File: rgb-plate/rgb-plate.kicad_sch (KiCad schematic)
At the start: 0 parts

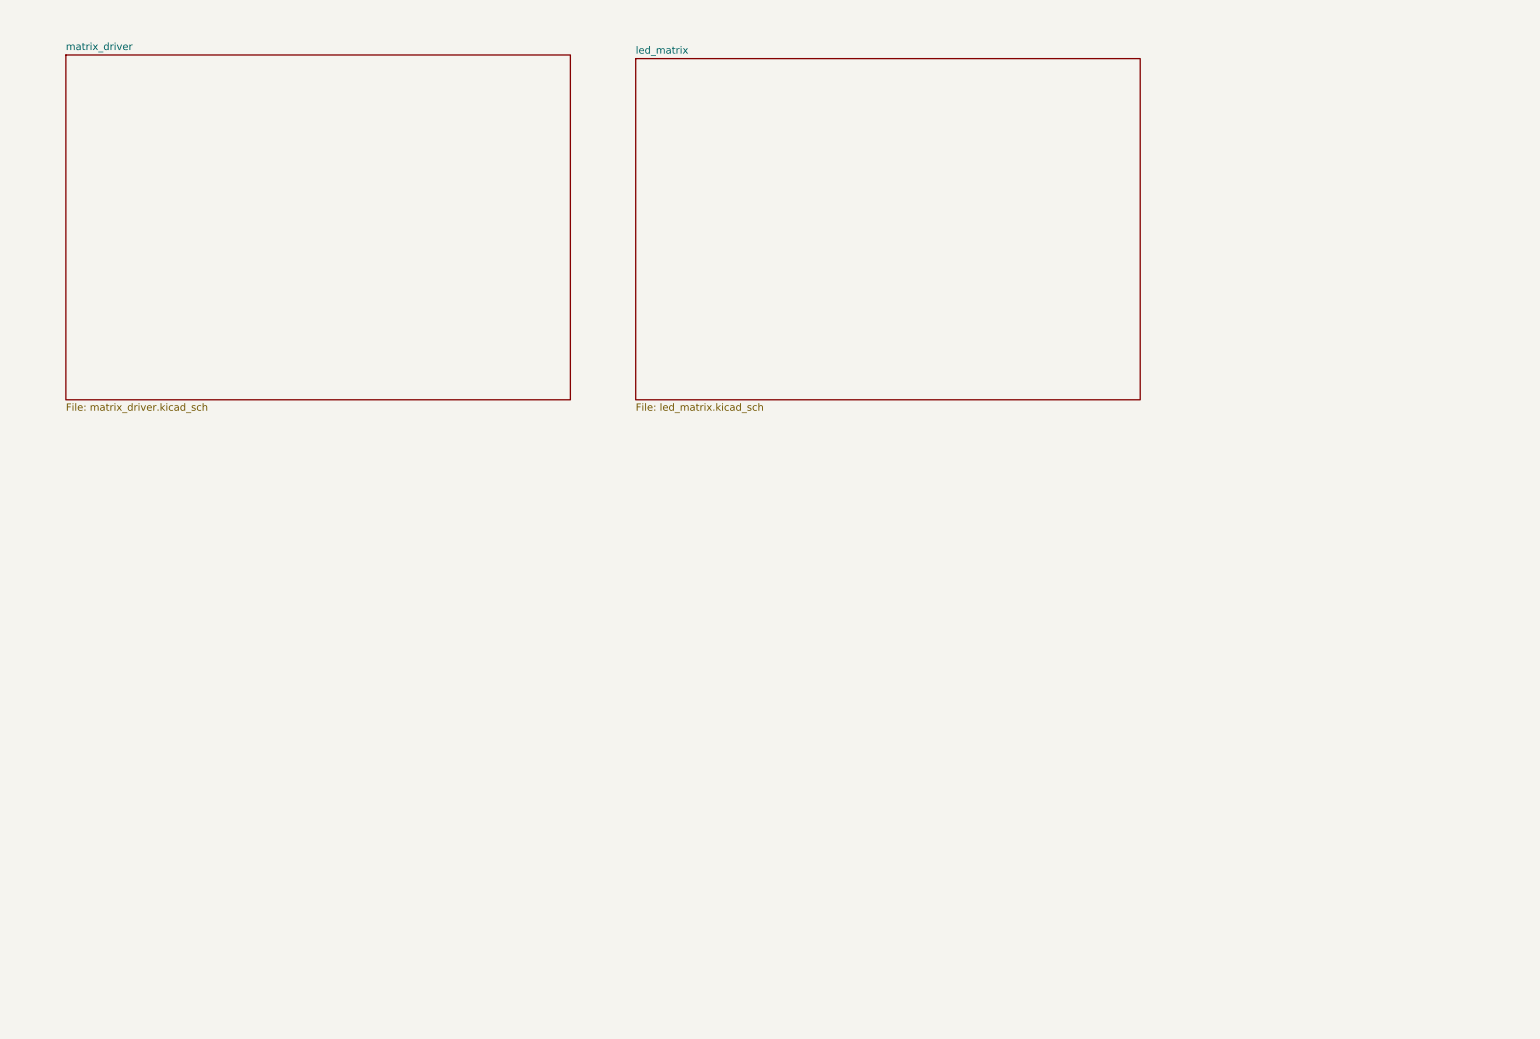
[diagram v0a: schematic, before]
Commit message: added additional sheets and leds with matrix driver and first regulator
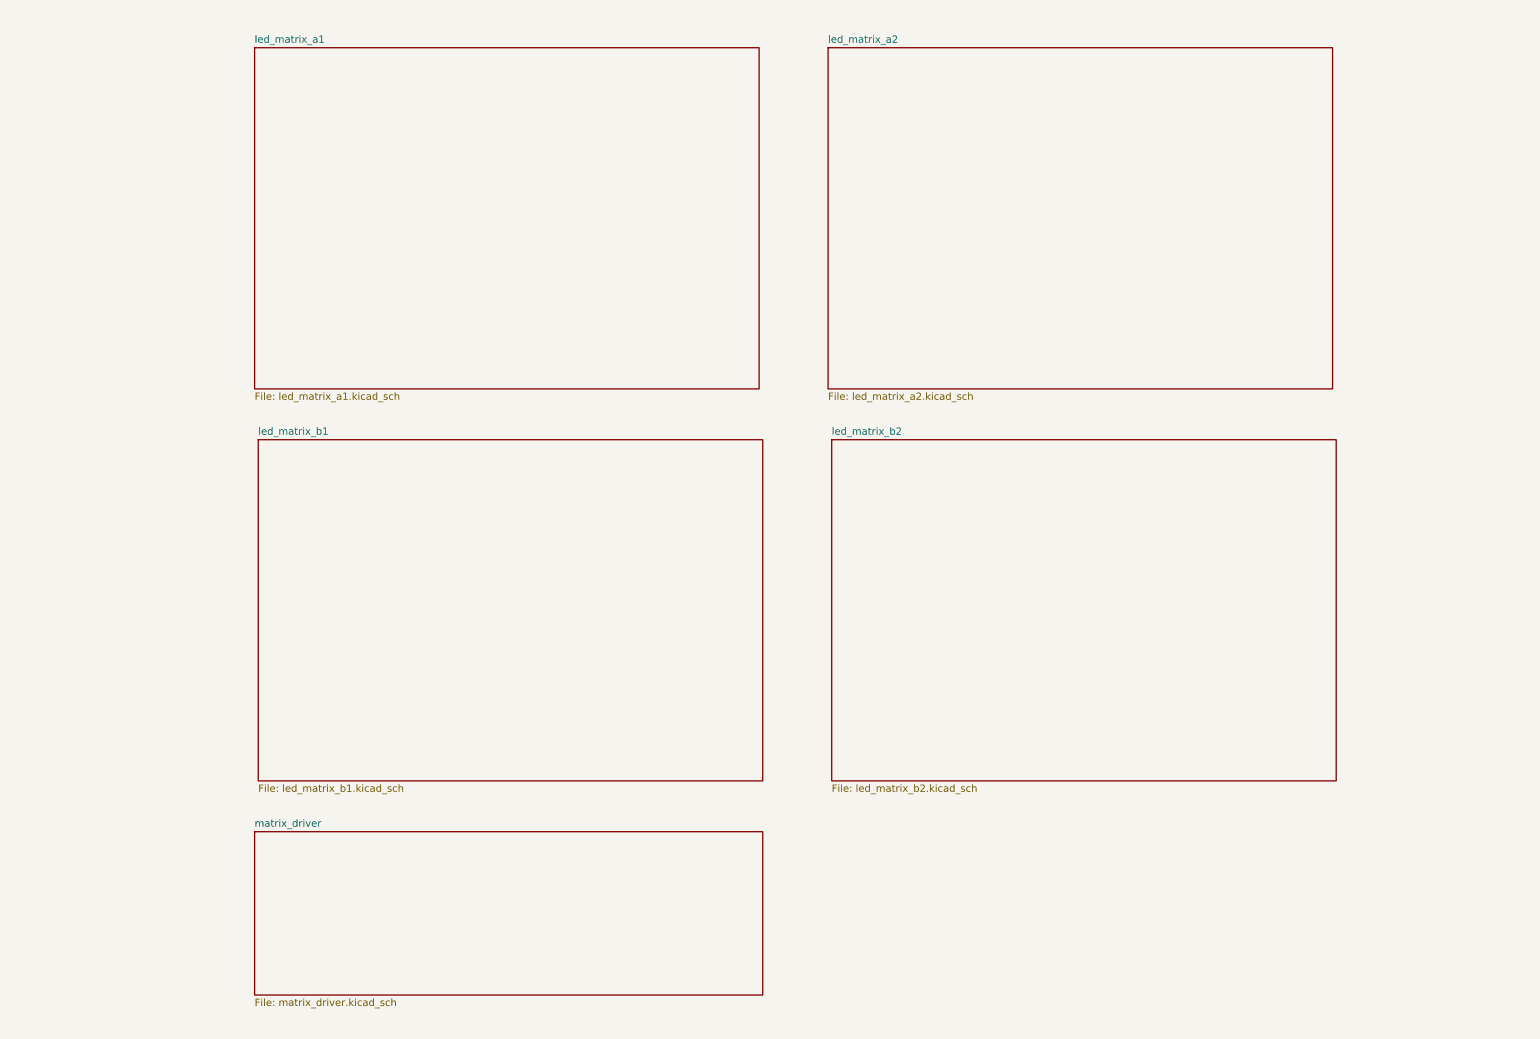
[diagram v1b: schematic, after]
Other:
- sheet led_matrix renamed led_matrix_a1
- added sheet led_matrix_a2 (led_matrix_a2.kicad_sch)
- added sheet led_matrix_b1 (led_matrix_b1.kicad_sch)
- added sheet led_matrix_b2 (led_matrix_b2.kicad_sch)
- sheet led_matrix_a1: file led_matrix.kicad_sch -> led_matrix_a1.kicad_sch
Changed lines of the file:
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@@
 	(paper "A4")
 	(sheet
-		(at 26.035 24.13)
-		(size 88.265 60.325)
+		(at 59.055 160.02)
+		(size 88.9 28.575)
 		(exclude_from_sim no)
 		(in_bom yes)
@@
 		)
 		(property "Sheetname" "matrix_driver"
-			(at 26.035 23.4184 0)
+			(at 59.055 159.3084 0)
 			(effects
 				(font
@@
 		)
 		(property "Sheetfile" "matrix_driver.kicad_sch"
-			(at 26.035 85.0396 0)
+			(at 59.055 189.1796 0)
 			(effects
 				(font
@@
 	)
 	(sheet
-		(at 125.73 24.765)
-		(size 88.265 59.69)
-		(exclude_from_sim no)
-		(in_bom yes)
-		(on_board yes)
-		(dnp no)
-		(fields_autoplaced yes)
-		(stroke
-			(width 0.1524)
-			(type solid)
-		)
-		(fill
-			(color 0 0 0 0.0000)
-		)
-		(property "Sheetname" "led_matrix"
-			(at 125.73 24.0534 0)
-			(effects
-				(font
-					(size 1.27 1.27)
-				)
-				(justify left bottom)
-			)
-		)
-		(property "Sheetfile" "led_matrix.kicad_sch"
-			(at 125.73 85.0396 0)
+		(at 59.055 22.86)
+		(size 88.265 59.69)
+		(exclude_from_sim no)
+		(in_bom yes)
+		(on_board yes)
+		(dnp no)
+		(fields_autoplaced yes)
+		(stroke
+			(width 0.1524)
+			(type solid)
+		)
+		(fill
+			(color 0 0 0 0.0000)
+		)
+		(property "Sheetname" "led_matrix_a1"
+			(at 59.055 22.1484 0)
+			(effects
+				(font
+					(size 1.27 1.27)
+				)
+				(justify left bottom)
+			)
+		)
+		(property "Sheetfile" "led_matrix_a1.kicad_sch"
+			(at 59.055 83.1346 0)
 			(effects
 				(font
@@
 				)
 			)
+		)
+	)
+	(sheet
+		(at 160.02 91.44)
+		(size 88.265 59.69)
+		(exclude_from_sim no)
+		(in_bom yes)
+		(on_board yes)
+		(dnp no)
+		(fields_autoplaced yes)
+		(stroke
+			(width 0.1524)
+			(type solid)
+		)
+		(fill
+			(color 0 0 0 0.0000)
+		)
+		(property "Sheetname" "led_matrix_b2"
+			(at 160.02 90.7284 0)
+			(effects
+				(font
+					(size 1.27 1.27)
+				)
+				(justify left bottom)
+			)
+		)
+		(property "Sheetfile" "led_matrix_b2.kicad_sch"
+			(at 160.02 151.7146 0)
+			(effects
+				(font
+					(size 1.27 1.27)
+				)
+				(justify left top)
+			)
+		)
+		(instances
+			(project "rgb-plate"
+				(path "/9c7e9324-2b76-44c1-9f0e-b92eb5faec31"
+					(page "6")
+				)
+			)
+		)
+	)
+	(sheet
+		(at 159.385 22.86)
+		(size 88.265 59.69)
+		(exclude_from_sim no)
+		(in_bom yes)
+		(on_board yes)
+		(dnp no)
+		(fields_autoplaced yes)
+		(stroke
+			(width 0.1524)
+			(type solid)
+		)
+		(fill
+			(color 0 0 0 0.0000)
+		)
+		(property "Sheetname" "led_matrix_a2"
+			(at 159.385 22.1484 0)
+			(effects
+				(font
+					(size 1.27 1.27)
+				)
+				(justify left bottom)
+			)
+		)
+		(property "Sheetfile" "led_matrix_a2.kicad_sch"
+			(at 159.385 83.1346 0)
+			(effects
+				(font
+					(size 1.27 1.27)
+				)
+				(justify left top)
+			)
+		)
+		(instances
+			(project "rgb-plate"
+				(path "/9c7e9324-2b76-44c1-9f0e-b92eb5faec31"
+					(page "4")
+				)
+			)
+		)
+	)
+	(sheet
+		(at 59.69 91.44)
+		(size 88.265 59.69)
+		(exclude_from_sim no)
+		(in_bom yes)
+		(on_board yes)
+		(dnp no)
+		(fields_autoplaced yes)
+		(stroke
+			(width 0.1524)
+			(type solid)
+		)
+		(fill
+			(color 0 0 0 0.0000)
+		)
+		(property "Sheetname" "led_matrix_b1"
+			(at 59.69 90.7284 0)
+			(effects
+				(font
+					(size 1.27 1.27)
+				)
+				(justify left bottom)
+			)
+		)
+		(property "Sheetfile" "led_matrix_b1.kicad_sch"
+			(at 59.69 151.7146 0)
+			(effects
+				(font
+					(size 1.27 1.27)
+				)
+				(justify left top)
+			)
+		)
+		(instances
+			(project "rgb-plate"
+				(path "/9c7e9324-2b76-44c1-9f0e-b92eb5faec31"
+					(page "5")
+				)
+			)

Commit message: initial layout on single board, may need to split up
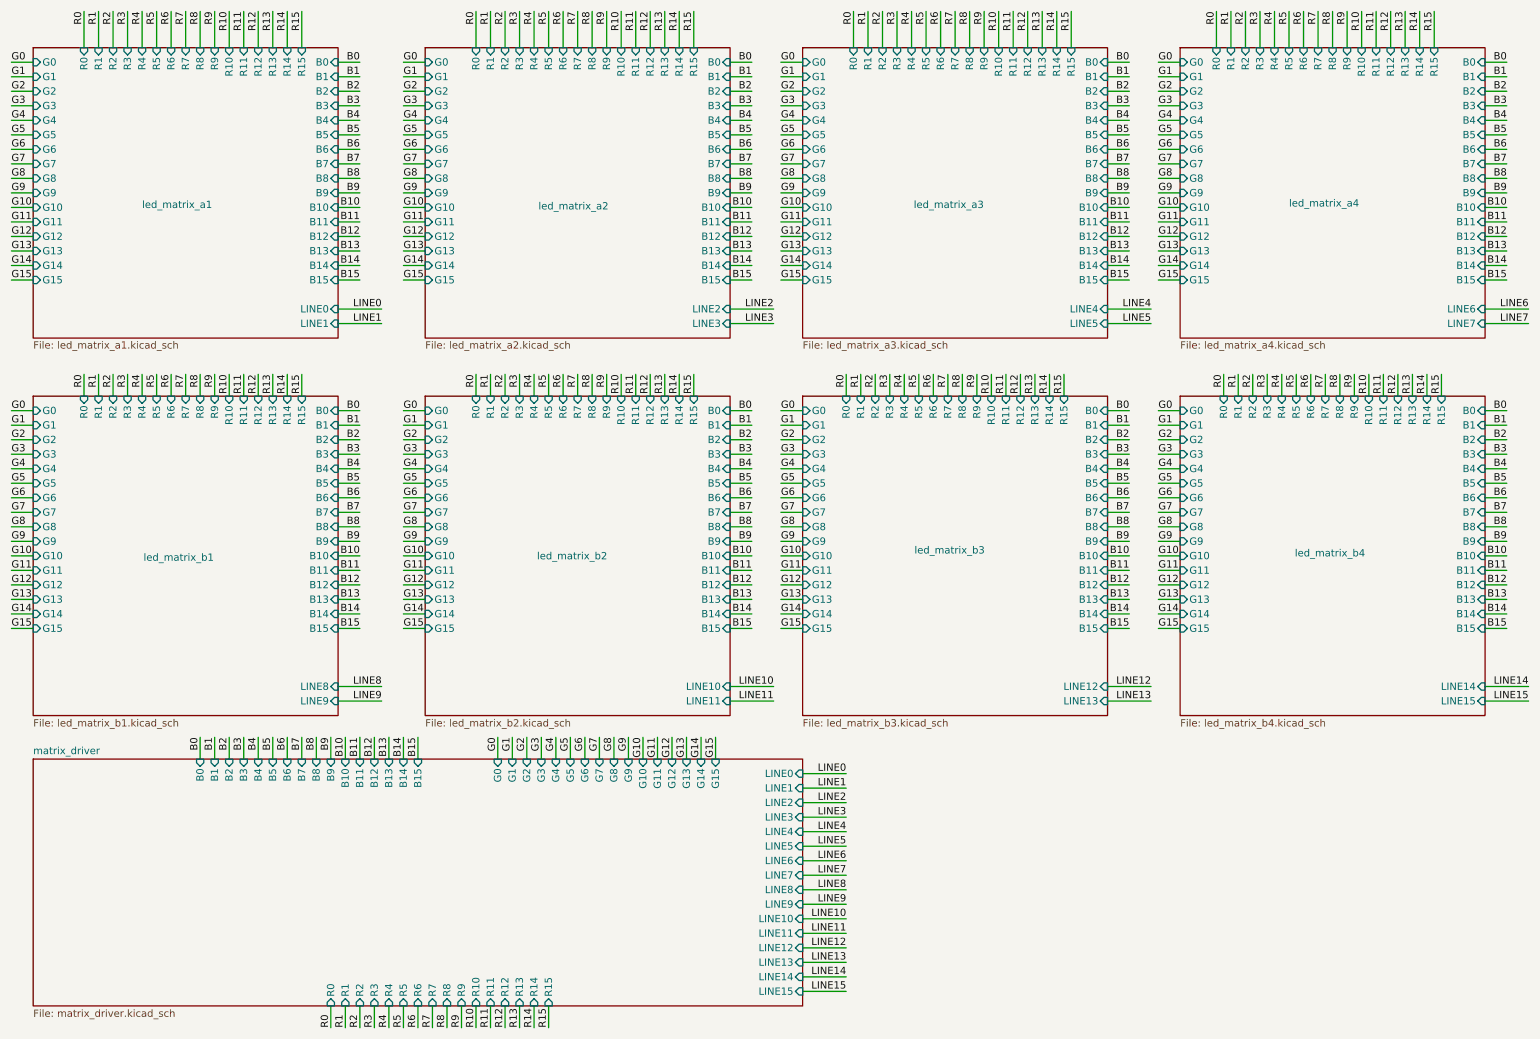
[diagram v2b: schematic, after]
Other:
- added sheet led_matrix_a3 (led_matrix_a3.kicad_sch)
- added sheet led_matrix_a4 (led_matrix_a4.kicad_sch)
- added sheet led_matrix_b3 (led_matrix_b3.kicad_sch)
- added sheet led_matrix_b4 (led_matrix_b4.kicad_sch)
- sheet led_matrix_a1 ports: added B0, B1, B10, B11, B12, B13, B14, B15, B2, B3, B4, B5, B6, B7, B8, B9, G0, G1, G10, G11, G12, G13, G14, G15, G2, G3, G4, G5, G6, G7, G8, G9, LINE0, LINE1, R0, R1, R10, R11, R12, R13, R14, R15, R2, R3, R4, R5, R6, R7, R8, R9; removed none
- sheet led_matrix_a2 ports: added B0, B1, B10, B11, B12, B13, B14, B15, B2, B3, B4, B5, B6, B7, B8, B9, G0, G1, G10, G11, G12, G13, G14, G15, G2, G3, G4, G5, G6, G7, G8, G9, LINE2, LINE3, R0, R1, R10, R11, R12, R13, R14, R15, R2, R3, R4, R5, R6, R7, R8, R9; removed none
- sheet led_matrix_b1 ports: added B0, B1, B10, B11, B12, B13, B14, B15, B2, B3, B4, B5, B6, B7, B8, B9, G0, G1, G10, G11, G12, G13, G14, G15, G2, G3, G4, G5, G6, G7, G8, G9, LINE8, LINE9, R0, R1, R10, R11, R12, R13, R14, R15, R2, R3, R4, R5, R6, R7, R8, R9; removed none
- sheet led_matrix_b2 ports: added B0, B1, B10, B11, B12, B13, B14, B15, B2, B3, B4, B5, B6, B7, B8, B9, G0, G1, G10, G11, G12, G13, G14, G15, G2, G3, G4, G5, G6, G7, G8, G9, LINE10, LINE11, R0, R1, R10, R11, R12, R13, R14, R15, R2, R3, R4, R5, R6, R7, R8, R9; removed none
- sheet matrix_driver ports: added B0, B1, B10, B11, B12, B13, B14, B15, B2, B3, B4, B5, B6, B7, B8, B9, G0, G1, G10, G11, G12, G13, G14, G15, G2, G3, G4, G5, G6, G7, G8, G9, LINE0, LINE1, LINE10, LINE11, LINE12, LINE13, LINE14, LINE15, LINE2, LINE3, LINE4, LINE5, LINE6, LINE7, LINE8, LINE9, R0, R1, R10, R11, R12, R13, R14, R15, R2, R3, R4, R5, R6, R7, R8, R9; removed none

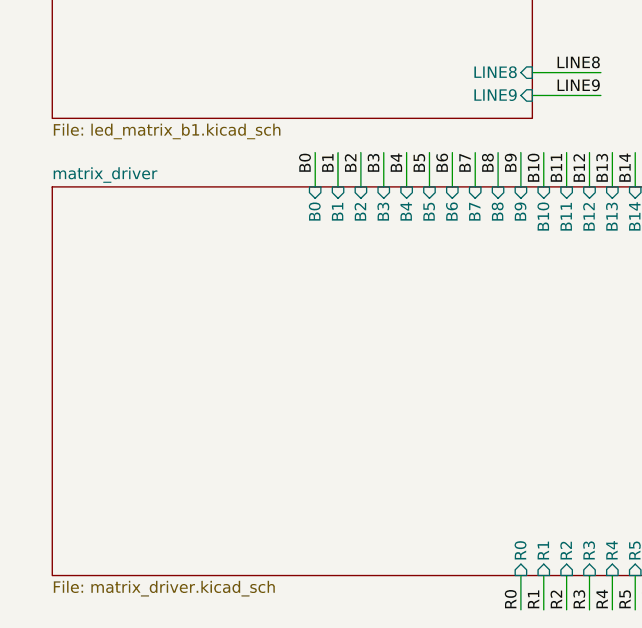
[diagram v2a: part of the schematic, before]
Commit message: update complete architecture to allow for improved routing scheme - separate boards for led plate and driver. adjusted matrix board to only hold leds and connectors and thermistors, created new board for driver
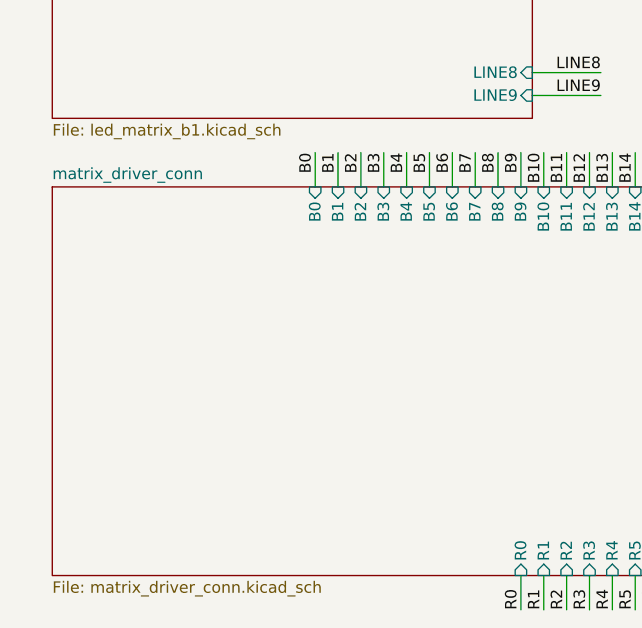
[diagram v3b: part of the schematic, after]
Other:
- sheet matrix_driver renamed matrix_driver_conn
- sheet matrix_driver_conn: file matrix_driver.kicad_sch -> matrix_driver_conn.kicad_sch
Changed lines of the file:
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@@
 			(color 0 0 0 0.0000)
 		)
-		(property "Sheetname" "matrix_driver"
+		(property "Sheetname" "matrix_driver_conn"
 			(at 20.32 146.6084 0)
 			(effects
@@
 			)
 		)
-		(property "Sheetfile" "matrix_driver.kicad_sch"
+		(property "Sheetfile" "matrix_driver_conn.kicad_sch"
 			(at 20.32 191.0846 0)
 			(effects
